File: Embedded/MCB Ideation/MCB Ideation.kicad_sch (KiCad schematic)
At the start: 22 parts, among them J1 USB, J2 Power, J3 MicroSD, J4 GPIO 0, U1 Sensored, U2 Expansion, U3 Comms Link Expansion, U4 AP7366-33W5-7

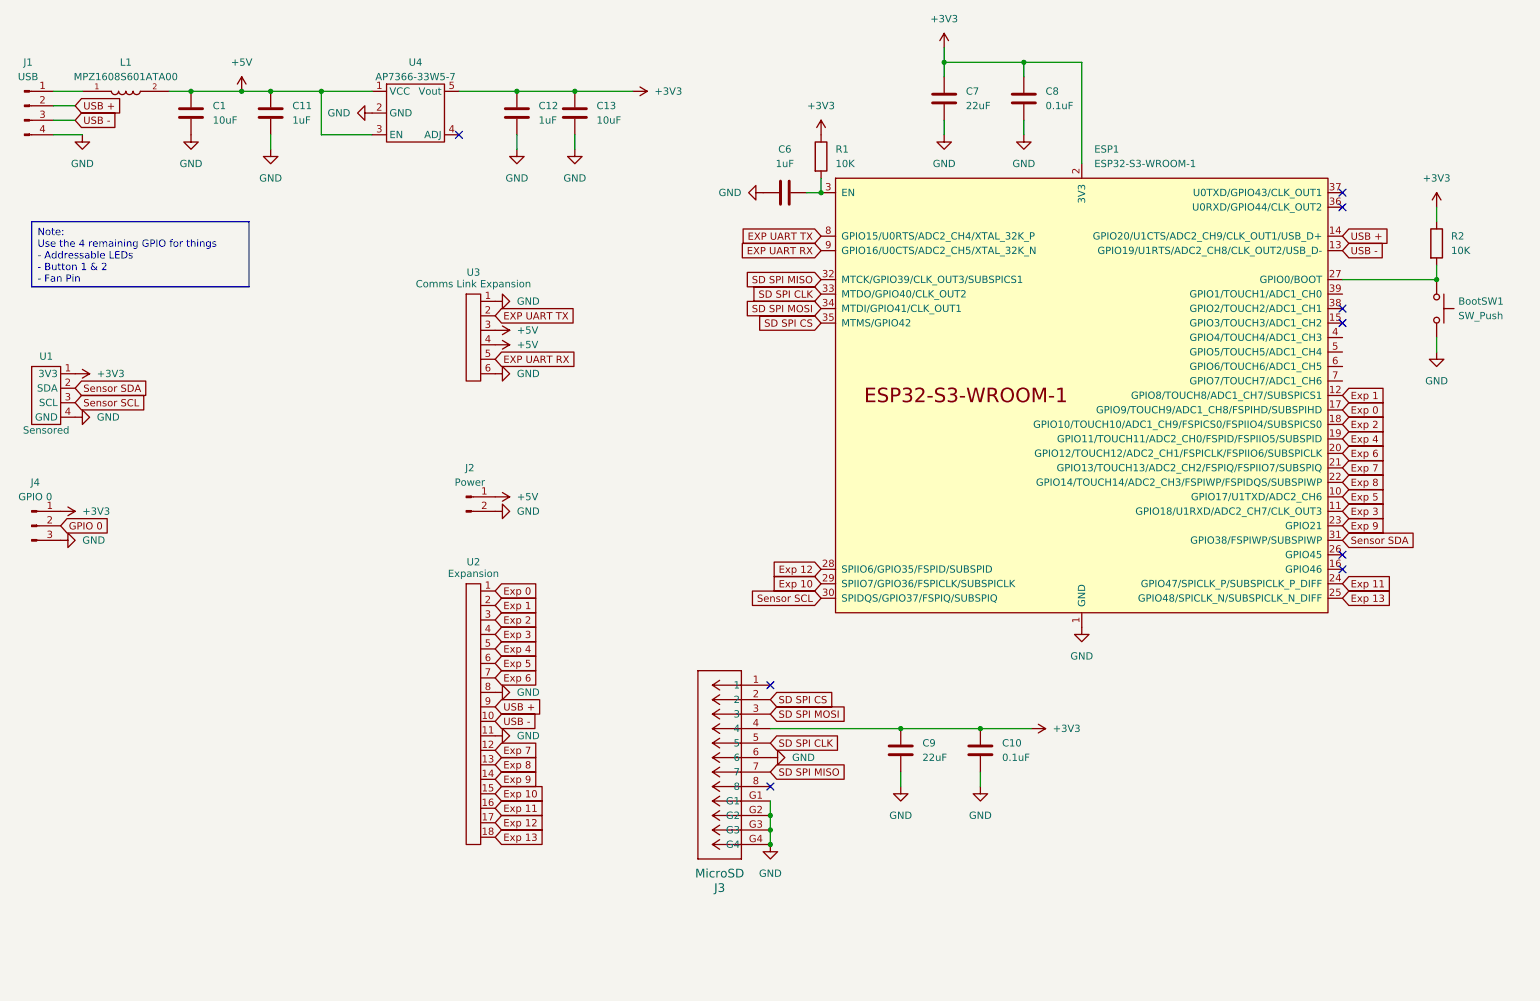
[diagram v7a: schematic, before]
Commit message: Added GPIO Pins
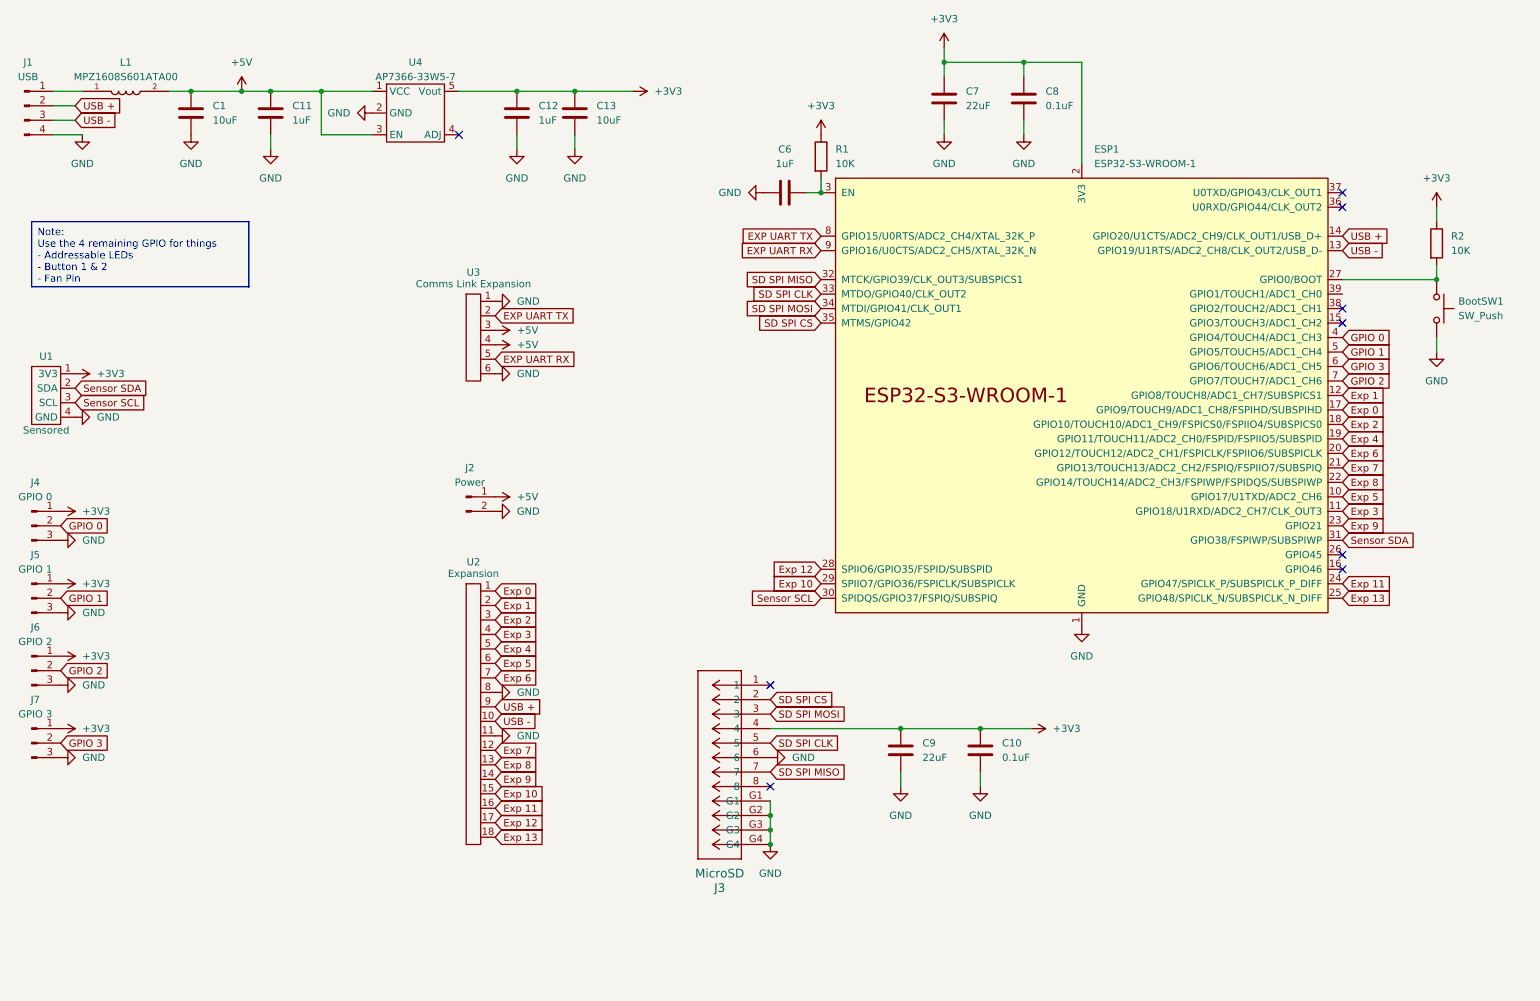
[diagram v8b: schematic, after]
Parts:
- added J5: GPIO 1, Connector_PinHeader_2.54mm:PinHeader_1x03_P2.54mm_Vertical, symbol Connector:Conn_01x03_Pin
- added J6: GPIO 2, Connector_PinHeader_2.54mm:PinHeader_1x03_P2.54mm_Vertical, symbol Connector:Conn_01x03_Pin
- added J7: GPIO 3, Connector_PinHeader_2.54mm:PinHeader_1x03_P2.54mm_Vertical, symbol Connector:Conn_01x03_Pin
- J4: footprint (none) -> Connector_PinHeader_2.54mm:PinHeader_1x03_P2.54mm_Vertical
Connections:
- net +3V3: now also J5.1 (Pin_1), J6.1 (Pin_1), J7.1 (Pin_1)
- net GND: now also J5.3 (Pin_3), J6.3 (Pin_3), J7.3 (Pin_3)
- net GPIO 0: now also ESP1.4 (GPIO4/TOUCH4/ADC1_CH3)
- net GPIO 1: now reaches ESP1.5 (GPIO5/TOUCH5/ADC1_CH4)
- net GPIO 1: now also J5.2 (Pin_2)
- net GPIO 3: now reaches ESP1.6 (GPIO6/TOUCH6/ADC1_CH5)
- net GPIO 3: now also J7.2 (Pin_2)
- net GPIO 2: now reaches ESP1.7 (GPIO7/TOUCH7/ADC1_CH6)
- net GPIO 2: now also J6.2 (Pin_2)
